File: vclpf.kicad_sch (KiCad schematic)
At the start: 38 parts, among them J1 NJ2FD-V, J2 NJ2FD-V, J3 NJ2FD-V, Q1 2N3904, Q2 2N3906, Q3 2N3904, Q4 2N3906, U1 ADA4084-4xCP, U2 ADA4084-4xCP

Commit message: cleanup
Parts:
- added C5: 1u, symbol Device:C
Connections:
- net at Q1.3 (C), Q2.3 (C): now also C5.2
- net at R11.2, U2.2 (+): now also C5.1
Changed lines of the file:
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@@
   (junction (at 30.48 109.22) (diameter 0) (color 0 0 0 0)
   )
+  (junction (at 109.22 27.94) (diameter 0) (color 0 0 0 0)
+  )
   (junction (at 139.7 27.94) (diameter 0) (color 0 0 0 0)
   )
@@
   (junction (at 45.72 87.63) (diameter 0) (color 0 0 0 0)
   )
+  (junction (at 109.22 35.56) (diameter 0) (color 0 0 0 0)
+  )
   (junction (at 29.21 80.01) (diameter 0) (color 0 0 0 0)
   )
@@
     (stroke (width 0) (type default))
   )
+  (wire (pts (xy 109.22 35.56) (xy 116.84 35.56))
+    (stroke (width 0) (type default))
+  )
   (wire (pts (xy 30.48 99.06) (xy 34.29 99.06))
     (stroke (width 0) (type default))
   )
+  (wire (pts (xy 109.22 27.94) (xy 123.19 27.94))
+    (stroke (width 0) (type default))
+  )
   (wire (pts (xy 101.6 45.72) (xy 110.49 45.72))
     (stroke (width 0) (type default))
@@
     (stroke (width 0) (type default))
   )
-  (wire (pts (xy 101.6 27.94) (xy 123.19 27.94))
-    (stroke (width 0) (type default))
-  )
-  (wire (pts (xy 101.6 35.56) (xy 116.84 35.56))
+  (wire (pts (xy 101.6 27.94) (xy 109.22 27.94))
+    (stroke (width 0) (type default))
+  )
+  (wire (pts (xy 101.6 35.56) (xy 109.22 35.56))
     (stroke (width 0) (type default))
   )
@@
       (effects (font (size 1.27 1.27)) hide)
     )
-    (property "Sim.Library" "C:\\Users\\Jan-Erik Matthies\\Documents\\kicad\\VCLPF\\spice\\ada4084_quad.txt" (at 93.98 68.58 0)
-      (effects (font (size 1.27 1.27)) hide)
-    )
-    (property "Sim.Name" "ADA4084c" (at 93.98 68.58 0)
+    (property "Sim.Library" "spice\\ada4084_quad.txt" (at 93.98 68.58 0)
+      (effects (font (size 1.27 1.27)) hide)
+    )
+    (property "Sim.Name" "ADA4084-4" (at 93.98 68.58 0)
       (effects (font (size 1.27 1.27)) hide)
     )
@@
       (effects (font (size 1.27 1.27)) hide)
     )
-    (property "Sim.Library" "C:\\Users\\Jan-Erik Matthies\\Documents\\kicad\\VCLPF\\spice\\ada4084_quad.txt" (at 162.56 71.12 0)
-      (effects (font (size 1.27 1.27)) hide)
-    )
-    (property "Sim.Name" "ADA4084c" (at 162.56 71.12 0)
+    (property "Sim.Library" "spice\\ada4084_quad.txt" (at 162.56 71.12 0)
+      (effects (font (size 1.27 1.27)) hide)
+    )
+    (property "Sim.Name" "ADA4084-4" (at 162.56 71.12 0)
       (effects (font (size 1.27 1.27)) hide)
     )
@@
       (effects (font (size 1.27 1.27)) hide)
     )
-    (property "Sim.Library" "C:\\Users\\Jan-Erik Matthies\\Documents\\kicad\\VCLPF\\spice\\ada4084_quad.txt" (at 58.42 27.94 0)
-      (effects (font (size 1.27 1.27)) hide)
-    )
-    (property "Sim.Name" "ADA4084c" (at 58.42 27.94 0)
+    (property "Sim.Library" "spice\\ada4084_quad.txt" (at 58.42 27.94 0)
+      (effects (font (size 1.27 1.27)) hide)
+    )
+    (property "Sim.Name" "ADA4084-4" (at 58.42 27.94 0)
       (effects (font (size 1.27 1.27)) hide)
     )
@@
       (effects (font (size 1.27 1.27)) hide)
     )
-    (property "Sim.Library" "C:\\Users\\Jan-Erik Matthies\\Documents\\kicad\\VCLPF\\spice\\ada4084_quad.txt" (at 124.46 69.85 0)
-      (effects (font (size 1.27 1.27)) hide)
-    )
-    (property "Sim.Name" "ADA4084c" (at 124.46 69.85 0)
+    (property "Sim.Library" "spice\\ada4084_quad.txt" (at 124.46 69.85 0)
+      (effects (font (size 1.27 1.27)) hide)
+    )
+    (property "Sim.Name" "ADA4084-4" (at 124.46 69.85 0)
       (effects (font (size 1.27 1.27)) hide)
     )
@@
       (effects (font (size 1.27 1.27)) hide)
     )
-    (property "Sim.Library" "C:\\Users\\Jan-Erik Matthies\\Documents\\kicad\\VCLPF\\spice\\ada4084_quad.txt" (at 193.04 71.12 0)
-      (effects (font (size 1.27 1.27)) hide)
-    )
-    (property "Sim.Name" "ADA4084c" (at 193.04 71.12 0)
+    (property "Sim.Library" "spice\\ada4084_quad.txt" (at 193.04 71.12 0)
+      (effects (font (size 1.27 1.27)) hide)
+    )
+    (property "Sim.Name" "ADA4084-4" (at 193.04 71.12 0)
       (effects (font (size 1.27 1.27)) hide)
     )
@@
       (effects (font (size 1.27 1.27)) hide)
     )
-    (property "Sim.Library" "C:\\Users\\Jan-Erik Matthies\\Documents\\kicad\\VCLPF\\spice\\ada4084_quad.txt" (at 54.61 80.01 0)
-      (effects (font (size 1.27 1.27)) hide)
-    )
-    (property "Sim.Name" "ADA4084c" (at 54.61 80.01 0)
+    (property "Sim.Library" "spice\\ada4084_quad.txt" (at 54.61 80.01 0)
+      (effects (font (size 1.27 1.27)) hide)
+    )
+    (property "Sim.Name" "ADA4084-4" (at 54.61 80.01 0)
       (effects (font (size 1.27 1.27)) hide)
     )
@@
       (effects (font (size 1.27 1.27)) (justify left) hide)
     )
-    (property "Sim.Library" "C:\\Users\\Jan-Erik Matthies\\Documents\\kicad\\VCLPF\\spice\\2N3906.LIB" (at 187.96 40.64 0)
+    (property "Sim.Library" "spice\\2N3906.LIB" (at 187.96 40.64 0)
       (effects (font (size 1.27 1.27)) hide)
     )
@@
       (effects (font (size 1.27 1.27)) hide)
     )
-    (property "Sim.Library" "C:\\Users\\Jan-Erik Matthies\\Documents\\kicad\\VCLPF\\spice\\ada4084_quad.txt" (at 55.88 62.23 0)
-      (effects (font (size 1.27 1.27)) hide)
-    )
-    (property "Sim.Name" "ADA4084c" (at 55.88 62.23 0)
+    (property "Sim.Library" "spice\\ada4084_quad.txt" (at 55.88 62.23 0)
+      (effects (font (size 1.27 1.27)) hide)
+    )
+    (property "Sim.Name" "ADA4084-4" (at 55.88 62.23 0)
       (effects (font (size 1.27 1.27)) hide)
     )
@@
     )
   )
+  (symbol (lib_id "Device:C") (at 109.22 31.75 0) (unit 1)
+    (in_bom yes) (on_board yes) (dnp no) (fields_autoplaced)
+    (property "Reference" "C5" (at 113.03 30.48 0)
+      (effects (font (size 1.27 1.27)) (justify left))
+    )
+    (property "Value" "1u" (at 113.03 33.02 0)
+      (effects (font (size 1.27 1.27)) (justify left))
+    )
+    (property "Footprint" "" (at 110.1852 35.56 0)
+      (effects (font (size 1.27 1.27)) hide)
+    )
+    (property "Datasheet" "~" (at 109.22 31.75 0)
+      (effects (font (size 1.27 1.27)) hide)
+    )
+    (property "Sim.Device" "C" (at 109.22 31.75 0)
+      (effects (font (size 1.27 1.27)) hide)
+    )
+    (property "Sim.Pins" "1=+ 2=-" (at 109.22 31.75 0)
+      (effects (font (size 1.27 1.27)) hide)
+    )
+    (pin "1")
+    (pin "2")
+    (instances
+      (project "vclpf"
+        (path "/a3725654-db03-4f99-b8a1-d5f8d49fee1f"
+          (reference "C5") (unit 1)
+        )
+      )
+    )
+  )
   (symbol (lib_id "power:GND") (at 119.38 59.69 0) (unit 1)
     (in_bom yes) (on_board yes) (dnp no) (fields_autoplaced)
@@
       (effects (font (size 1.27 1.27)) (justify left) hide)
     )
-    (property "Sim.Library" "C:\\Users\\Jan-Erik Matthies\\Documents\\kicad\\VCLPF\\spice\\2N3904.LIB" (at 99.06 40.64 0)
+    (property "Sim.Library" "spice\\2N3904.LIB" (at 99.06 40.64 0)
       (effects (font (size 1.27 1.27)) hide)
     )
@@
       (effects (font (size 1.27 1.27)) hide)
     )
-    (property "Sim.Library" "C:\\Users\\Jan-Erik Matthies\\Documents\\kicad\\VCLPF\\spice\\ada4084_quad.txt" (at 130.81 27.94 0)
-      (effects (font (size 1.27 1.27)) hide)
-    )
-    (property "Sim.Name" "ADA4084c" (at 130.81 27.94 0)
+    (property "Sim.Library" "spice\\ada4084_quad.txt" (at 130.81 27.94 0)
+      (effects (font (size 1.27 1.27)) hide)
+    )
+    (property "Sim.Name" "ADA4084-4" (at 130.81 27.94 0)
       (effects (font (size 1.27 1.27)) hide)
     )
@@
       (effects (font (size 1.27 1.27)) (justify left) hide)
     )
-    (property "Sim.Library" "C:\\Users\\Jan-Erik Matthies\\Documents\\kicad\\VCLPF\\spice\\2N3904.LIB" (at 167.64 40.64 0)
+    (property "Sim.Library" "spice\\2N3904.LIB" (at 167.64 40.64 0)
       (effects (font (size 1.27 1.27)) hide)
     )
@@
       (effects (font (size 1.27 1.27)) hide)
     )
-    (property "Sim.Library" "C:\\Users\\Jan-Erik Matthies\\Documents\\kicad\\VCLPF\\spice\\ada4084_quad.txt" (at 45.72 80.01 0)
-      (effects (font (size 1.27 1.27)) hide)
-    )
-    (property "Sim.Name" "ADA4084c" (at 45.72 80.01 0)
+    (property "Sim.Library" "spice\\ada4084_quad.txt" (at 45.72 80.01 0)
+      (effects (font (size 1.27 1.27)) hide)
+    )
+    (property "Sim.Name" "ADA4084-4" (at 45.72 80.01 0)
       (effects (font (size 1.27 1.27)) hide)
     )
@@
       (effects (font (size 1.27 1.27)) hide)
     )
-    (property "Sim.Library" "C:\\Users\\Jan-Erik Matthies\\Documents\\kicad\\VCLPF\\spice\\ada4084_quad.txt" (at 199.39 27.94 0)
-      (effects (font (size 1.27 1.27)) hide)
-    )
-    (property "Sim.Name" "ADA4084c" (at 199.39 27.94 0)
+    (property "Sim.Library" "spice\\ada4084_quad.txt" (at 199.39 27.94 0)
+      (effects (font (size 1.27 1.27)) hide)
+    )
+    (property "Sim.Name" "ADA4084-4" (at 199.39 27.94 0)
       (effects (font (size 1.27 1.27)) hide)
     )
@@
       (effects (font (size 1.27 1.27)) (justify left) hide)
     )
-    (property "Sim.Library" "C:\\Users\\Jan-Erik Matthies\\Documents\\kicad\\VCLPF\\spice\\2N3906.LIB" (at 119.38 40.64 0)
-      (effects (font (size 1.27 1.27)) hide)
-    )
+    (property "Sim.Library" "spice\\2N3906.LIB" (at 119.38 40.64 0)
+      (effects (font (size 1.27 1.27)) hide)
+    )

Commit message: add schottkey
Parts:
- added D5, D6: BAT54S, Package_TO_SOT_SMD:SOT-23, symbol Diode:BAT54S
- R14, R17: value 10k -> 200k
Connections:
- new net: D6.1 (A), Q4.3 (C)
- new net: C5.2, D5.3 (COM)
- new net: D5.1 (A), Q2.3 (C)
- new net: D5.2 (K), Q1.3 (C)
- new net: C3.2, D6.3 (COM)
- new net: D6.2 (K), Q3.3 (C)
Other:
- moved on the sheet: C3, Q1, Q2, Q3, Q4, R12, R13, R19, R20, R23, R24, R25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

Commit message: optimize
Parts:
- C3: value 10u -> 1u
- C5: value 1u -> 0.1u
- R4: value 100k -> 50k
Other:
- moved on the sheet: R4
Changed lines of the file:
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@@
   (junction (at 109.22 27.94) (diameter 0) (color 0 0 0 0)
   )
+  (junction (at 162.56 69.85) (diameter 0) (color 0 0 0 0)
+  )
+  (junction (at 44.45 59.69) (diameter 0) (color 0 0 0 0)
+  )
+  (junction (at 193.04 69.85) (diameter 0) (color 0 0 0 0)
+  )
   (junction (at 139.7 27.94) (diameter 0) (color 0 0 0 0)
   )
-  (junction (at 162.56 69.85) (diameter 0) (color 0 0 0 0)
-  )
-  (junction (at 44.45 59.69) (diameter 0) (color 0 0 0 0)
-  )
-  (junction (at 193.04 69.85) (diameter 0) (color 0 0 0 0)
-  )
   (junction (at 45.72 72.39) (diameter 0) (color 0 0 0 0)
   )
@@
   (junction (at 45.72 87.63) (diameter 0) (color 0 0 0 0)
   )
-  (junction (at 107.95 90.17) (diameter 0) (color 0 0 0 0)
-  )
   (junction (at 29.21 80.01) (diameter 0) (color 0 0 0 0)
   )
@@
     (stroke (width 0) (type default))
   )
+  (wire (pts (xy 107.95 91.44) (xy 107.95 92.71))
+    (stroke (width 0) (type default))
+  )
   (wire (pts (xy 168.91 27.94) (xy 177.8 27.94))
     (stroke (width 0) (type default))
@@
     (stroke (width 0) (type default))
   )
+  (wire (pts (xy 139.7 27.94) (xy 161.29 27.94))
+    (stroke (width 0) (type default))
+  )
   (wire (pts (xy 115.57 85.09) (xy 121.92 85.09))
     (stroke (width 0) (type default))
@@
     (stroke (width 0) (type default))
   )
-  (wire (pts (xy 107.95 90.17) (xy 107.95 88.9))
-    (stroke (width 0) (type default))
-  )
   (wire (pts (xy 48.26 69.85) (xy 48.26 64.77))
     (stroke (width 0) (type default))
@@
     (stroke (width 0) (type default))
   )
-  (wire (pts (xy 139.7 27.94) (xy 161.29 27.94))
-    (stroke (width 0) (type default))
-  )
   (wire (pts (xy 177.8 27.94) (xy 191.77 27.94))
     (stroke (width 0) (type default))
@@
     (stroke (width 0) (type default))
   )
-  (wire (pts (xy 107.95 96.52) (xy 107.95 105.41))
+  (wire (pts (xy 107.95 100.33) (xy 107.95 105.41))
     (stroke (width 0) (type default))
   )
@@
       (effects (font (size 1.27 1.27)) hide)
     )
-    (property "Sim.Params" "dc=0 ampl=10 f=1000 td=0 theta=0 phase=0 ac=10" (at 19.05 25.4 0)
+    (property "Sim.Params" "dc=0 ampl=10 f=100 td=0 theta=0 phase=0 ac=10" (at 19.05 25.4 0)
       (effects (font (size 1.27 1.27)) hide)
     )
@@
       (effects (font (size 1.27 1.27)) (justify left))
     )
-    (property "Value" "1u" (at 113.03 33.02 0)
+    (property "Value" "0.1u" (at 113.03 33.02 0)
       (effects (font (size 1.27 1.27)) (justify left))
     )
@@
       (effects (font (size 1.27 1.27)) (justify left))
     )
-    (property "Value" "10u" (at 181.61 33.02 0)
+    (property "Value" "1u" (at 181.61 33.02 0)
       (effects (font (size 1.27 1.27)) (justify left))
     )
@@
     )
   )
-  (symbol (lib_id "Device:R") (at 107.95 92.71 180) (unit 1)
+  (symbol (lib_id "Device:R") (at 107.95 96.52 180) (unit 1)
     (in_bom yes) (on_board yes) (dnp no)
-    (property "Reference" "R4" (at 105.41 93.98 0)
-      (effects (font (size 1.27 1.27)) (justify left))
-    )
-    (property "Value" "100k" (at 105.41 93.98 0)
-      (effects (font (size 1.27 1.27)) (justify left))
-    )
-    (property "Footprint" "" (at 109.728 92.71 90)
-      (effects (font (size 1.27 1.27)) hide)
-    )
-    (property "Datasheet" "~" (at 107.95 92.71 0)
-      (effects (font (size 1.27 1.27)) hide)
-    )
-    (property "Sim.Device" "R" (at 107.95 92.71 0)
-      (effects (font (size 1.27 1.27)) hide)
-    )
-    (property "Sim.Pins" "1=+ 2=-" (at 107.95 92.71 0)
-      (effects (font (size 1.27 1.27)) hide)
-    )
+    (property "Reference" "R4" (at 105.41 97.79 0)
+      (effects (font (size 1.27 1.27)) (justify left))
+    )
+    (property "Value" "50k" (at 105.41 97.79 0)
+      (effects (font (size 1.27 1.27)) (justify left))
+    )
+    (property "Footprint" "" (at 109.728 96.52 90)
+      (effects (font (size 1.27 1.27)) hide)
+    )
+    (property "Datasheet" "~" (at 107.95 96.52 0)
+      (effects (font (size 1.27 1.27)) hide)
+    )
+    (property "Sim.Device" "R" (at 107.95 96.52 0)
+      (effects (font (size 1.27 1.27)) hide)
+    )
+    (property "Sim.Pins" "1=+ 2=-" (at 107.95 96.52 0)
+      (effects (font (size 1.27 1.27)) hide)
+    )

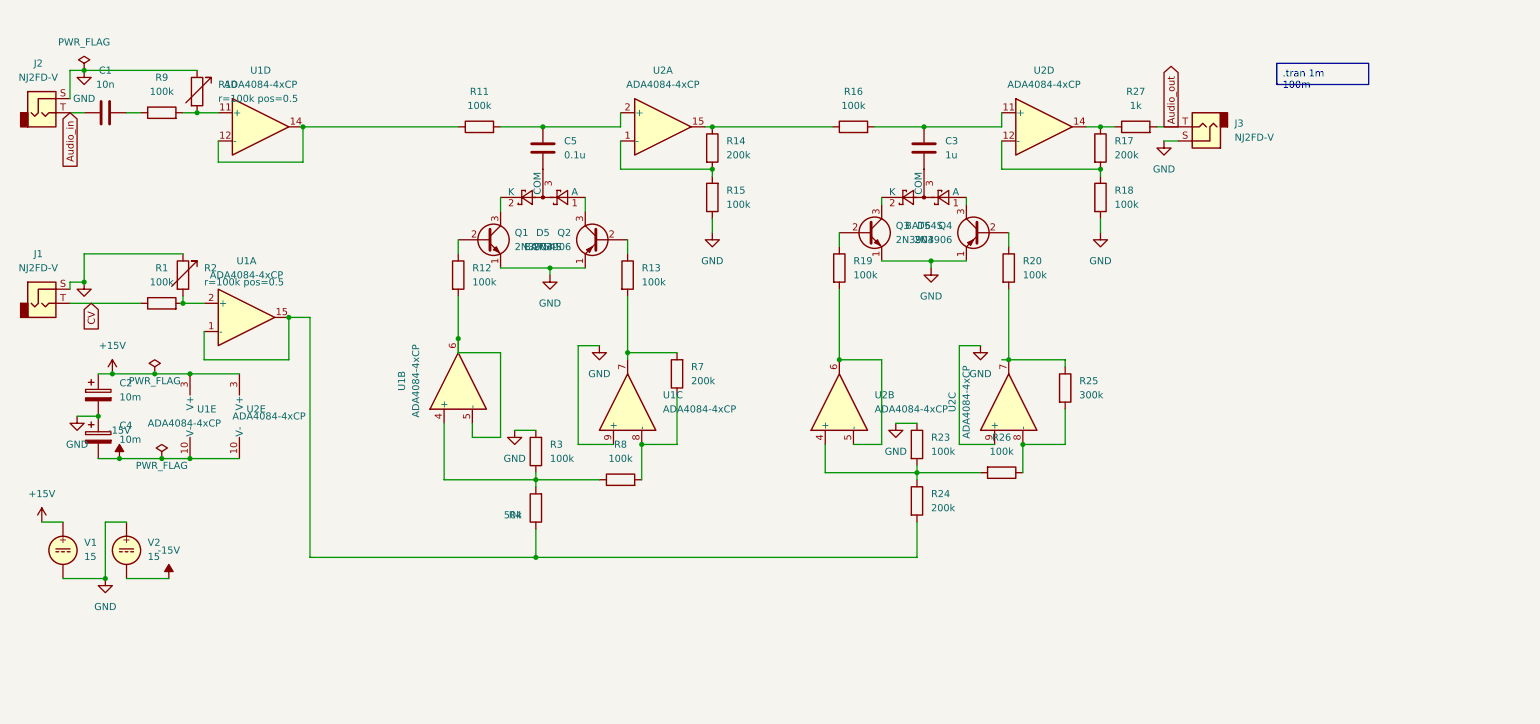
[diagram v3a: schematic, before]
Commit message: move diods to base
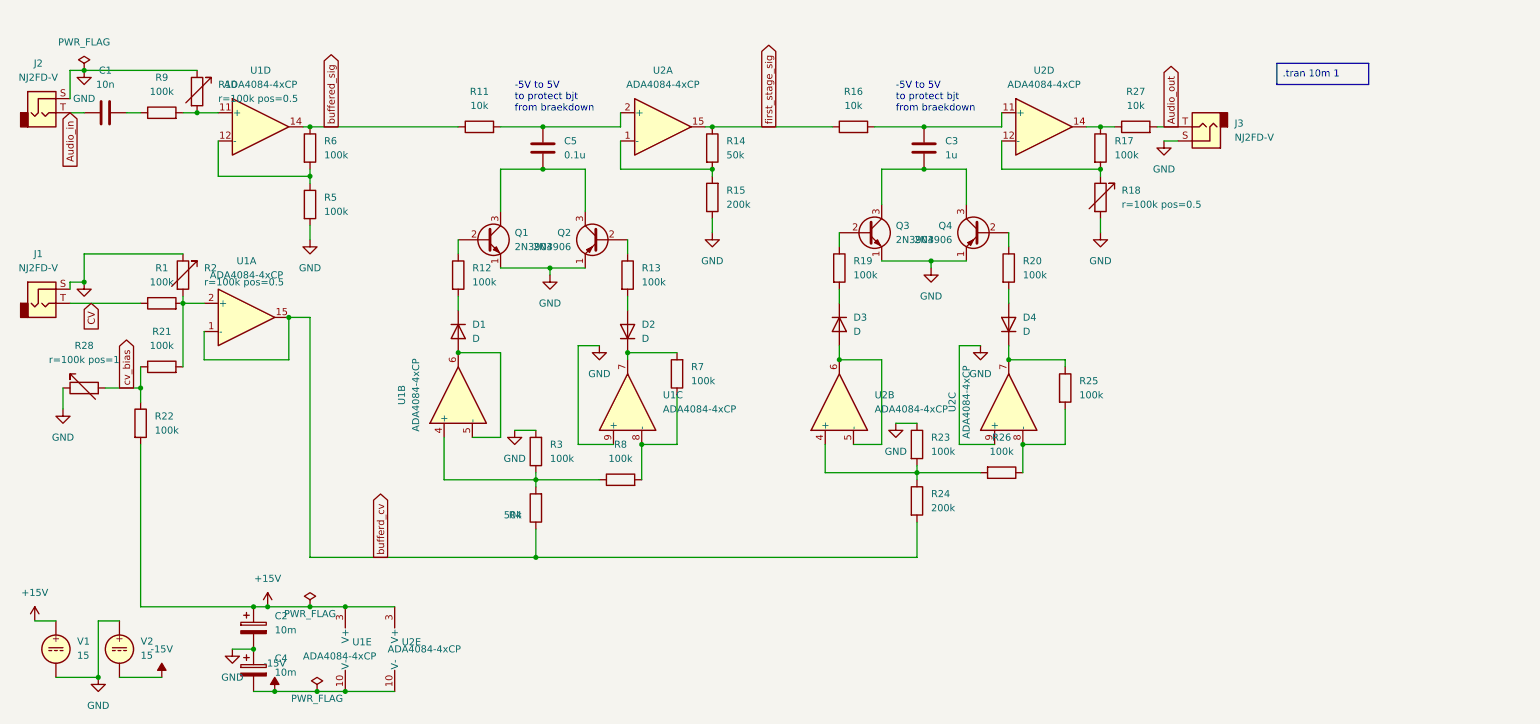
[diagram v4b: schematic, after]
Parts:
- removed D5, D6: BAT54S, Package_TO_SOT_SMD:SOT-23, symbol Diode:BAT54S
- removed R18: 100k, symbol Device:R
- added D1, D2, D3, D4: D, symbol Device:D
- added R18, R28: ${SIM.PARAMS}, symbol Device:R_Variable
- added R21, R22, R5, R6: 100k, symbol Device:R
- R11, R16: value 100k -> 10k
- R14: value 200k -> 50k
- R15: value 100k -> 200k
- R17, R7: value 200k -> 100k
- R25: value 300k -> 100k
- R27: value 1k -> 10k
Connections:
- net +15V: now also R22.2
- net GND: now also R18.2, R28.1, R5.2
- net at U1.5 (-), U1.6: now also D1.2 (A); no longer R12.2
- net bufferd_cv: now reaches R24.2, R4.1, U1.1 (-), U1.15
- net at U2.5 (-), U2.6: now also D3.2 (A); no longer R19.2
- net at R17.2, U2.12 (-): now also R18.1
- net buffered_sig: now reaches R11.1, U1.14
- net buffered_sig: now also R6.1; no longer U1.12 (-)
- net at R25.1, U2.7: now also D4.1 (K); no longer R20.2
- net at R7.2, U1.7: now also D2.1 (K); no longer R13.2
- net first_stage_sig: now reaches R14.1, R16.1, U2.15
- net at R1.2, R2.2, U1.2 (+): now also R21.2
- net at Q4.3 (C): now also C3.2, Q3.3 (C)
- net at C5.2: now also Q1.3 (C), Q2.3 (C)
- new net: D1.1 (K), R12.2
- new net: R5.1, R6.2, U1.12 (-)
- new net: D4.2 (A), R20.2
- new net: D2.2 (A), R13.2
- new net: D3.1 (K), R19.2
- new net cv_bias: R21.1, R22.1, R28.2
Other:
- note added: "-5V to 5V to protect bjt from braekdown"
- moved on the sheet: C2, C4, U1B, U1E, U2E, V1, V2
